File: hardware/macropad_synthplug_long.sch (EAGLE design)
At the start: 13 parts, among them IC1 H11L1MS, J1 SJ-3523-SMT, J2 SJ-3523-SMT

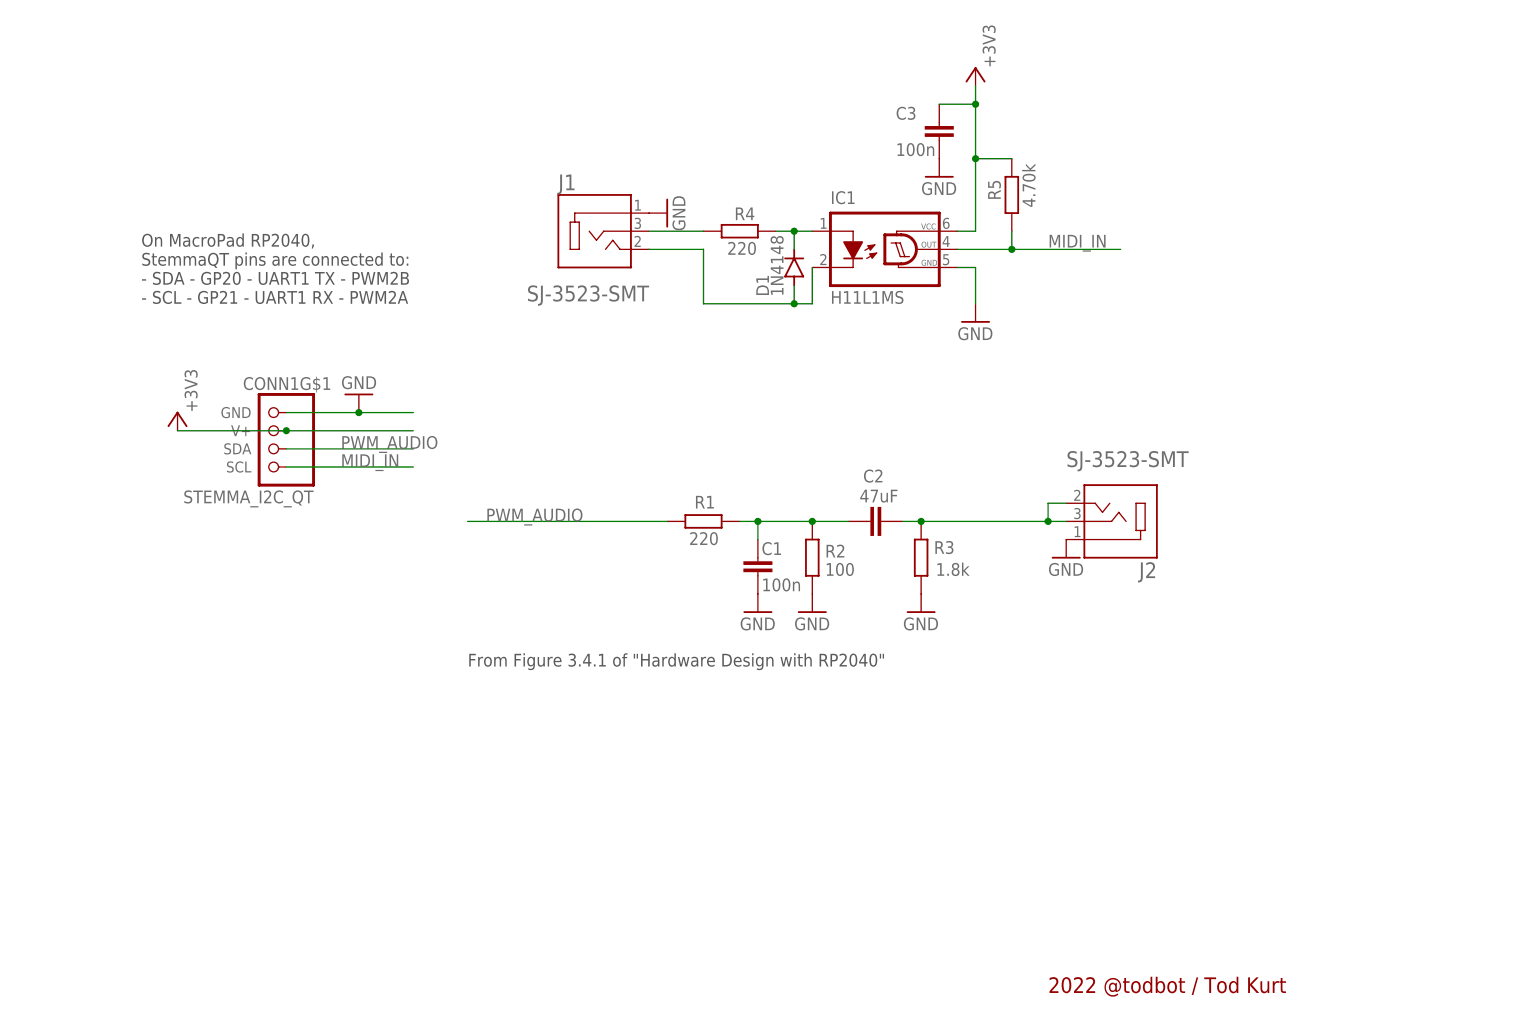
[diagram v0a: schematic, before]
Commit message: submit long version to fab
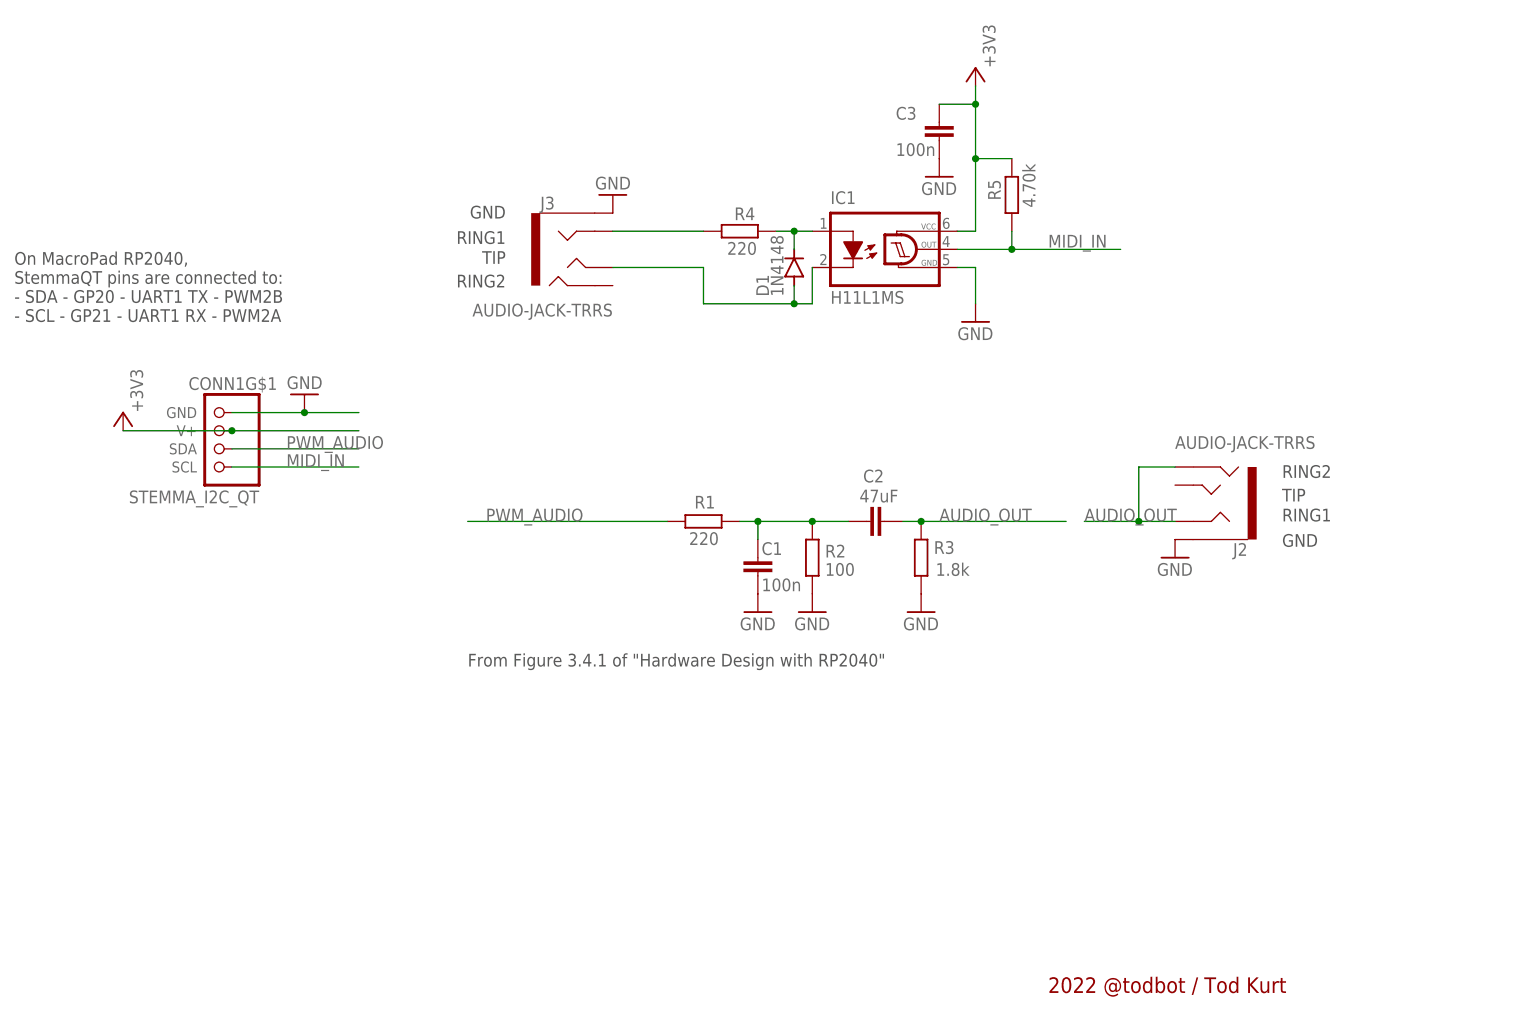
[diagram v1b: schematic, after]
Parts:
- removed J1: SJ-3523-SMT, SJ-3523-SMT:SJ-3523-SMT
- added J3: AUDIO-JACK-TRRS, audio_jacks_todbot:AUDIO-JACK-TRRS
- CONN1: LCSC2 (none) -> C160404; MPN (none) -> HC-1.0-4PWT; MPN2 (none) -> SM04B-SRSS-TB
- IC1: LCSC (none) -> C78589; MPN2 (none) -> H11L1S
- J2: value SJ-3523-SMT -> AUDIO-JACK-TRRS; device SJ-3523-SMT:SJ-3523-SMT -> audio_jacks_todbot:AUDIO-JACK-TRRS; LCSC (none) -> C431535
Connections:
- removed net N$15: J1.3, R4.2
- removed net N$47: C2.2, J2.2, J2.3, R3.1
- new net AUDIO_OUT: C2.2, J2.RING1, J2.RING2, R3.1
- new net N$2: J3.RING1, R4.2
- net GND: now also J2.EARTH, J3.EARTH; no longer J1.1, J2.1
- net N$14: now also J3.TIP; no longer J1.2
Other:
- note added: "GND"
- note added: "RING1"
- note added: "RING2"
- note added: "TIP"
- moved on the sheet: CONN1G$1

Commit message: crap
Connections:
- net AUDIO_OUT: now also J2.TIP; no longer J2.RING2
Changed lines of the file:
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@@
 <pinref part="J2" gate="G$1" pin="RING1"/>
 <wire x1="88.9" y1="43.18" x2="83.82" y2="43.18" width="0.1524" layer="91"/>
-<pinref part="J2" gate="G$1" pin="RING2"/>
-<wire x1="88.9" y1="50.8" x2="83.82" y2="50.8" width="0.1524" layer="91"/>
-<wire x1="83.82" y1="43.18" x2="83.82" y2="50.8" width="0.1524" layer="91"/>
+<wire x1="83.82" y1="43.18" x2="83.82" y2="48.26" width="0.1524" layer="91"/>
 <wire x1="83.82" y1="43.18" x2="76.2" y2="43.18" width="0.1524" layer="91"/>
 <junction x="83.82" y="43.18"/>
 <label x="76.2" y="43.18" size="1.778" layer="95"/>
+<pinref part="J2" gate="G$1" pin="TIP"/>
+<wire x1="88.9" y1="48.26" x2="83.82" y2="48.26" width="0.1524" layer="91"/>
 </segment>
 </net>

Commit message: get the trrs pinout right for realsies yeesh
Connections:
- net GND: now also J2.RING2
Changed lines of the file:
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@@
 <part name="J3" library="audio_jacks_todbot" deviceset="AUDIO-JACK-TRRS" device=""/>
 <part name="GND1" library="supply1" library_urn="urn:adsk.eagle:library:371" deviceset="GND" device=""/>
+<part name="GND3" library="supply1" library_urn="urn:adsk.eagle:library:371" deviceset="GND" device=""/>
 </parts>
 <sheets>
@@
 <attribute name="LCSC" x="99.06" y="45.72" size="1.778" layer="96" rot="R180" display="off"/>
 </instance>
-<instance part="GND2" gate="1" x="88.9" y="38.1" smashed="yes">
-<attribute name="VALUE" x="86.36" y="35.56" size="1.778" layer="96"/>
+<instance part="GND2" gate="1" x="83.82" y="38.1" smashed="yes">
+<attribute name="VALUE" x="81.28" y="35.56" size="1.778" layer="96"/>
 </instance>
 <instance part="J3" gate="G$1" x="0" y="81.28" smashed="yes">
@@
 <instance part="GND1" gate="1" x="10.16" y="88.9" smashed="yes" rot="R180">
 <attribute name="VALUE" x="12.7" y="91.44" size="1.778" layer="96" rot="R180"/>
+</instance>
+<instance part="GND3" gate="1" x="83.82" y="53.34" smashed="yes" rot="R180">
+<attribute name="VALUE" x="86.36" y="55.88" size="1.778" layer="96" rot="R180"/>
 </instance>
 </instances>
@@
 <pinref part="J2" gate="G$1" pin="EARTH"/>
 <pinref part="GND2" gate="1" pin="GND"/>
+<wire x1="83.82" y1="40.64" x2="88.9" y2="40.64" width="0.1524" layer="91"/>
 </segment>
 <segment>
@@
 <pinref part="GND1" gate="1" pin="GND"/>
 </segment>
+<segment>
+<pinref part="J2" gate="G$1" pin="RING2"/>
+<pinref part="GND3" gate="1" pin="GND"/>
+<wire x1="83.82" y1="50.8" x2="88.9" y2="50.8" width="0.1524" layer="91"/>
+</segment>
 </net>

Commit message: monosynth1 mostly works
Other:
- note added: "Works with cell phone earphones & stereo cables. Does not work w/ mono cables"
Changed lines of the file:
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@@
 <text x="-4.826" y="87.376" size="1.778" layer="97" rot="R180">GND</text>
 <text x="-4.826" y="81.026" size="1.778" layer="97" rot="R180">TIP</text>
+<text x="71.12" y="30.48" size="1.778" layer="97">Works with cell phone earphones &amp;
+stereo cables. Does not work w/ mono cables</text>
 </plain>
 <instances>
